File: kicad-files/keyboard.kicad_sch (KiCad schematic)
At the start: 148 parts, among them J1 TYPE-C-31-M12_13, U1 STM32F103x8_B-LQFP48

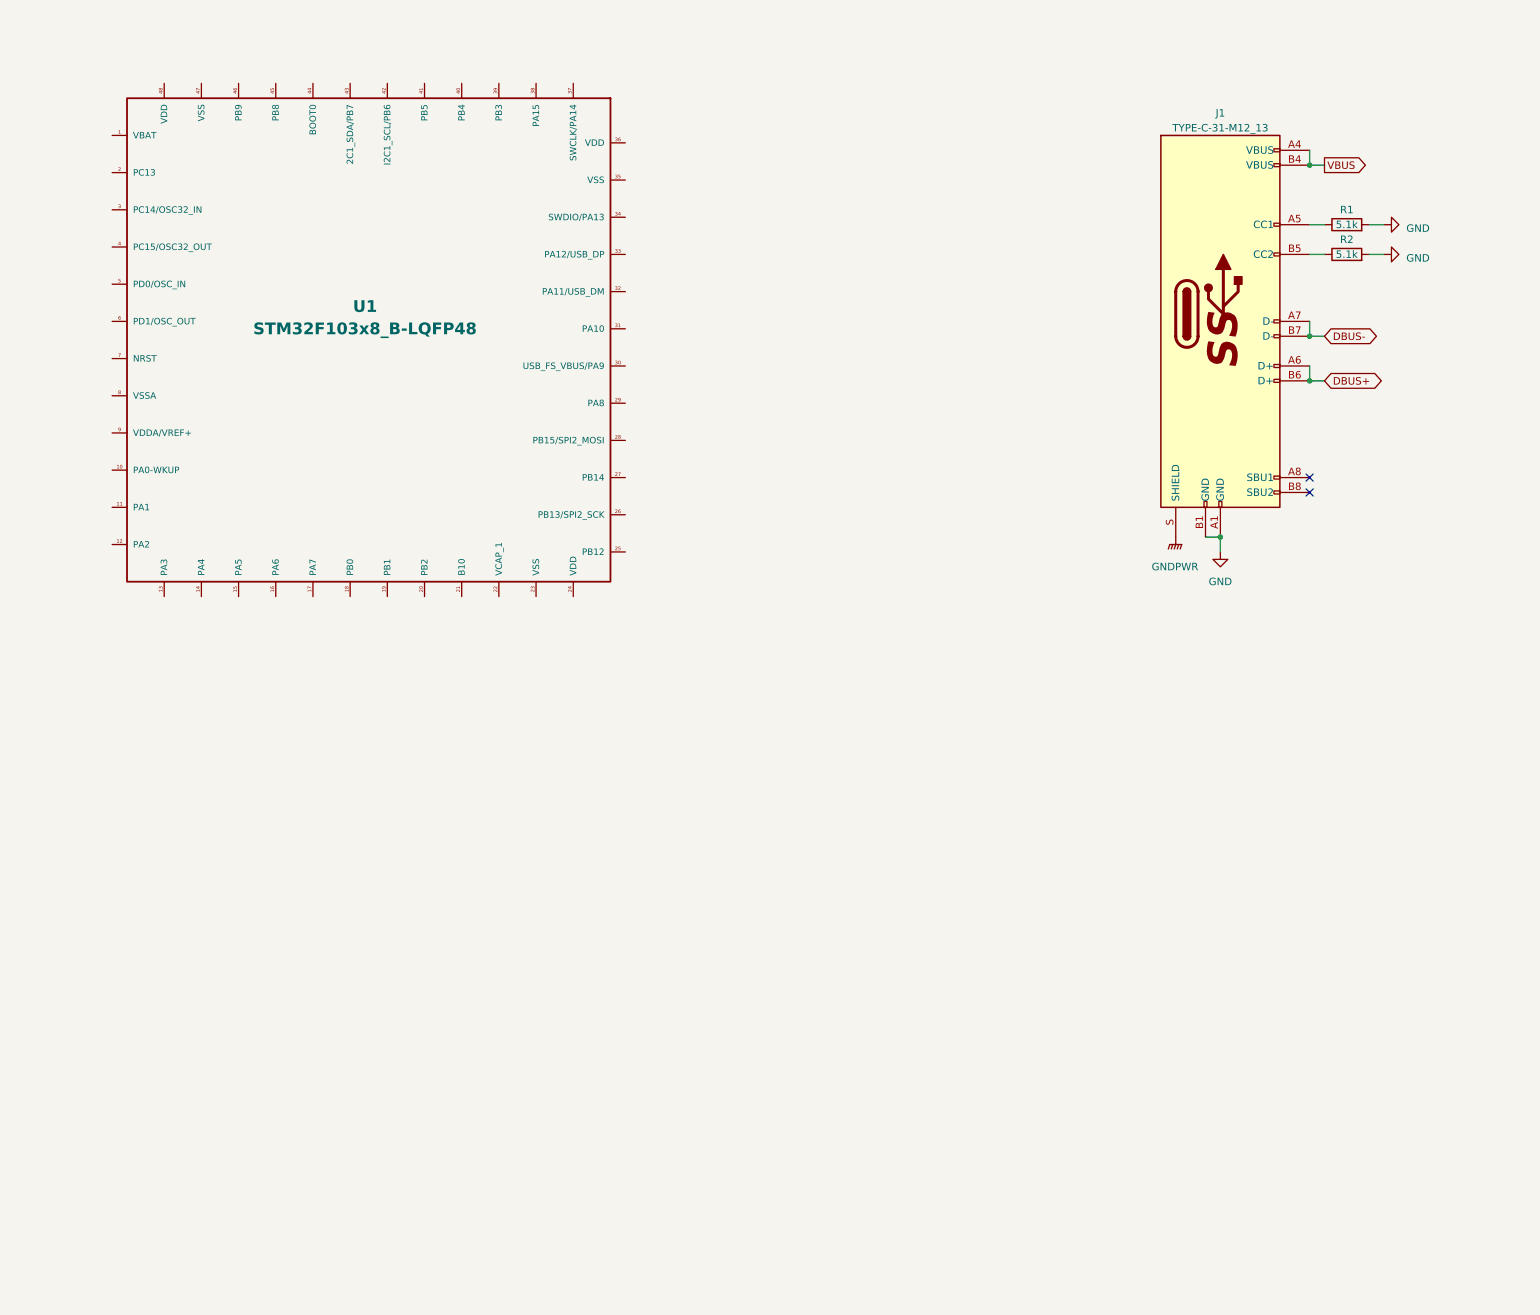
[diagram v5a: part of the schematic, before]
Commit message: Connected usb GNDPWR to inductor
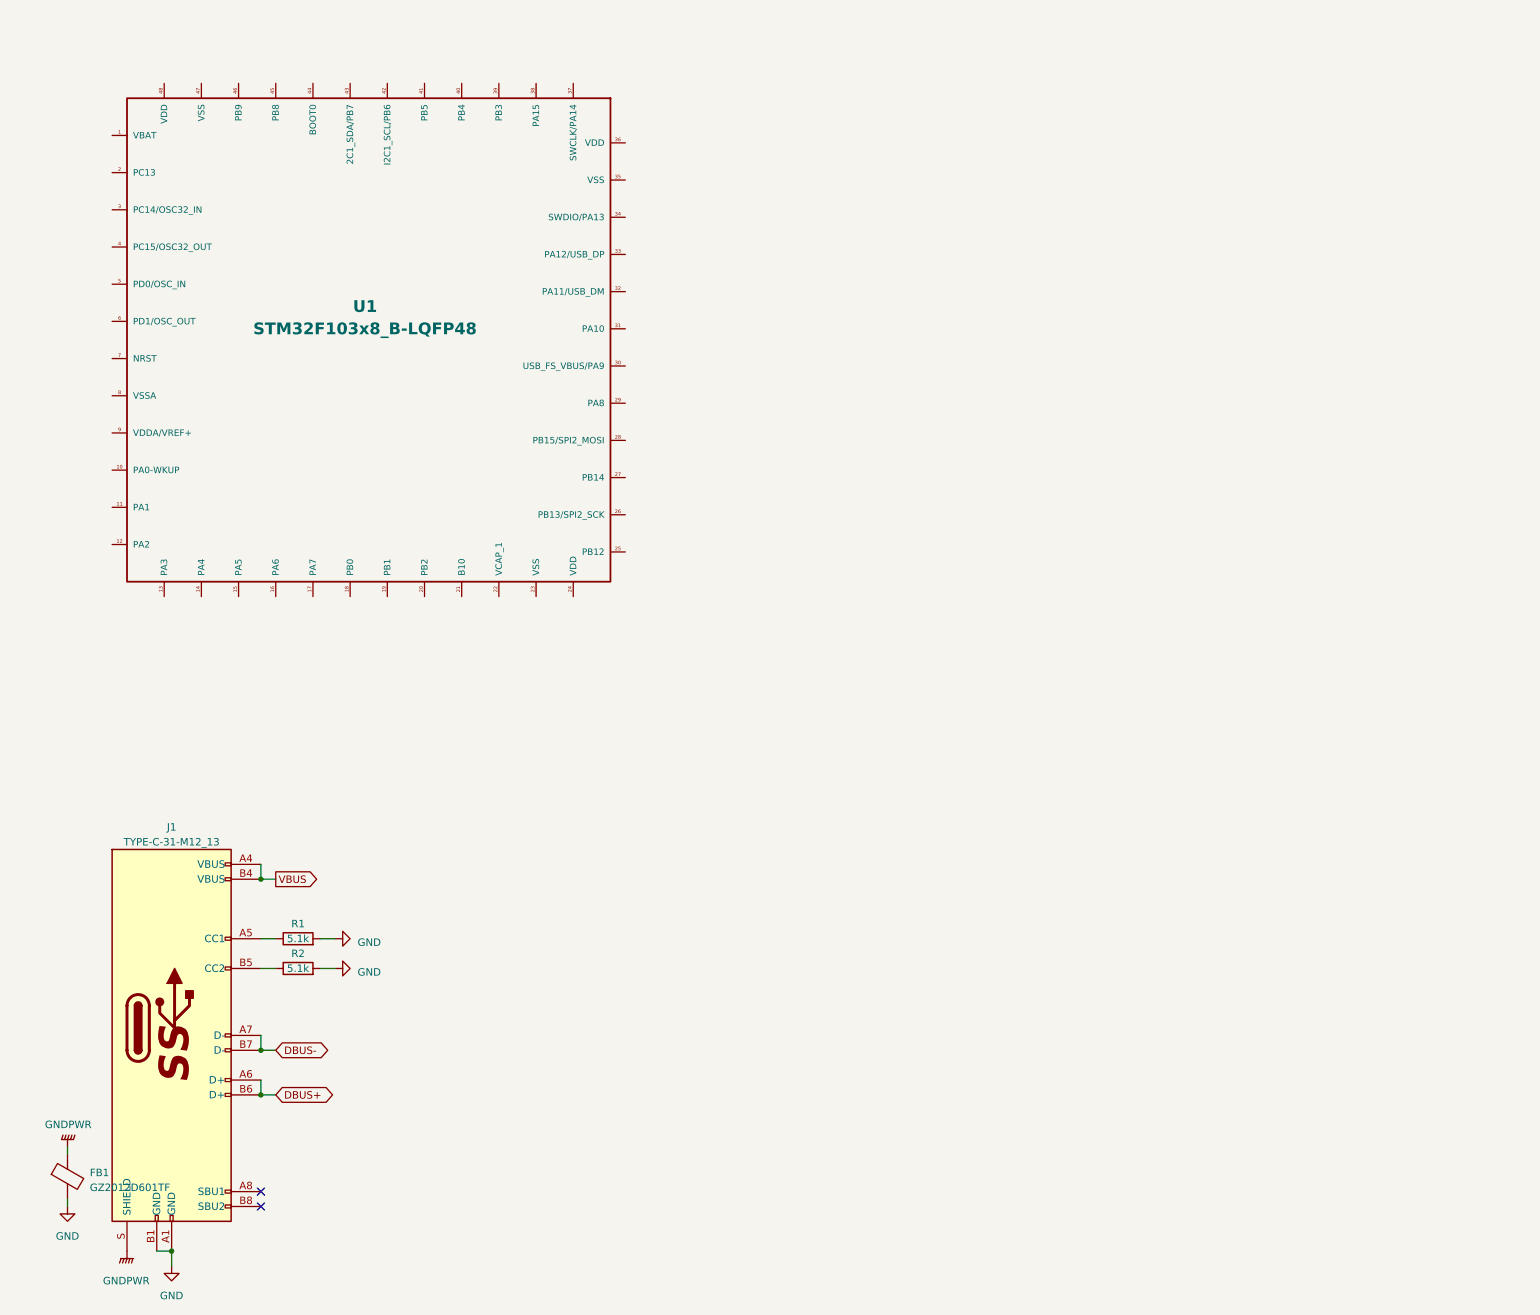
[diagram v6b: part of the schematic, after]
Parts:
- added FB1: GZ2012D601TF, Inductor_SMD:L_0805_2012Metric_Pad1.05x1.20mm_HandSolder, symbol Device:FerriteBead
- R1, R2: footprint Resistor_SMD:R_0805_2012Metric -> Resistor_SMD:R_0603_1608Metric
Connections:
- net GND: now also FB1.2
- net GNDPWR: now also FB1.1
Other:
- moved on the sheet: J1, R1, R2

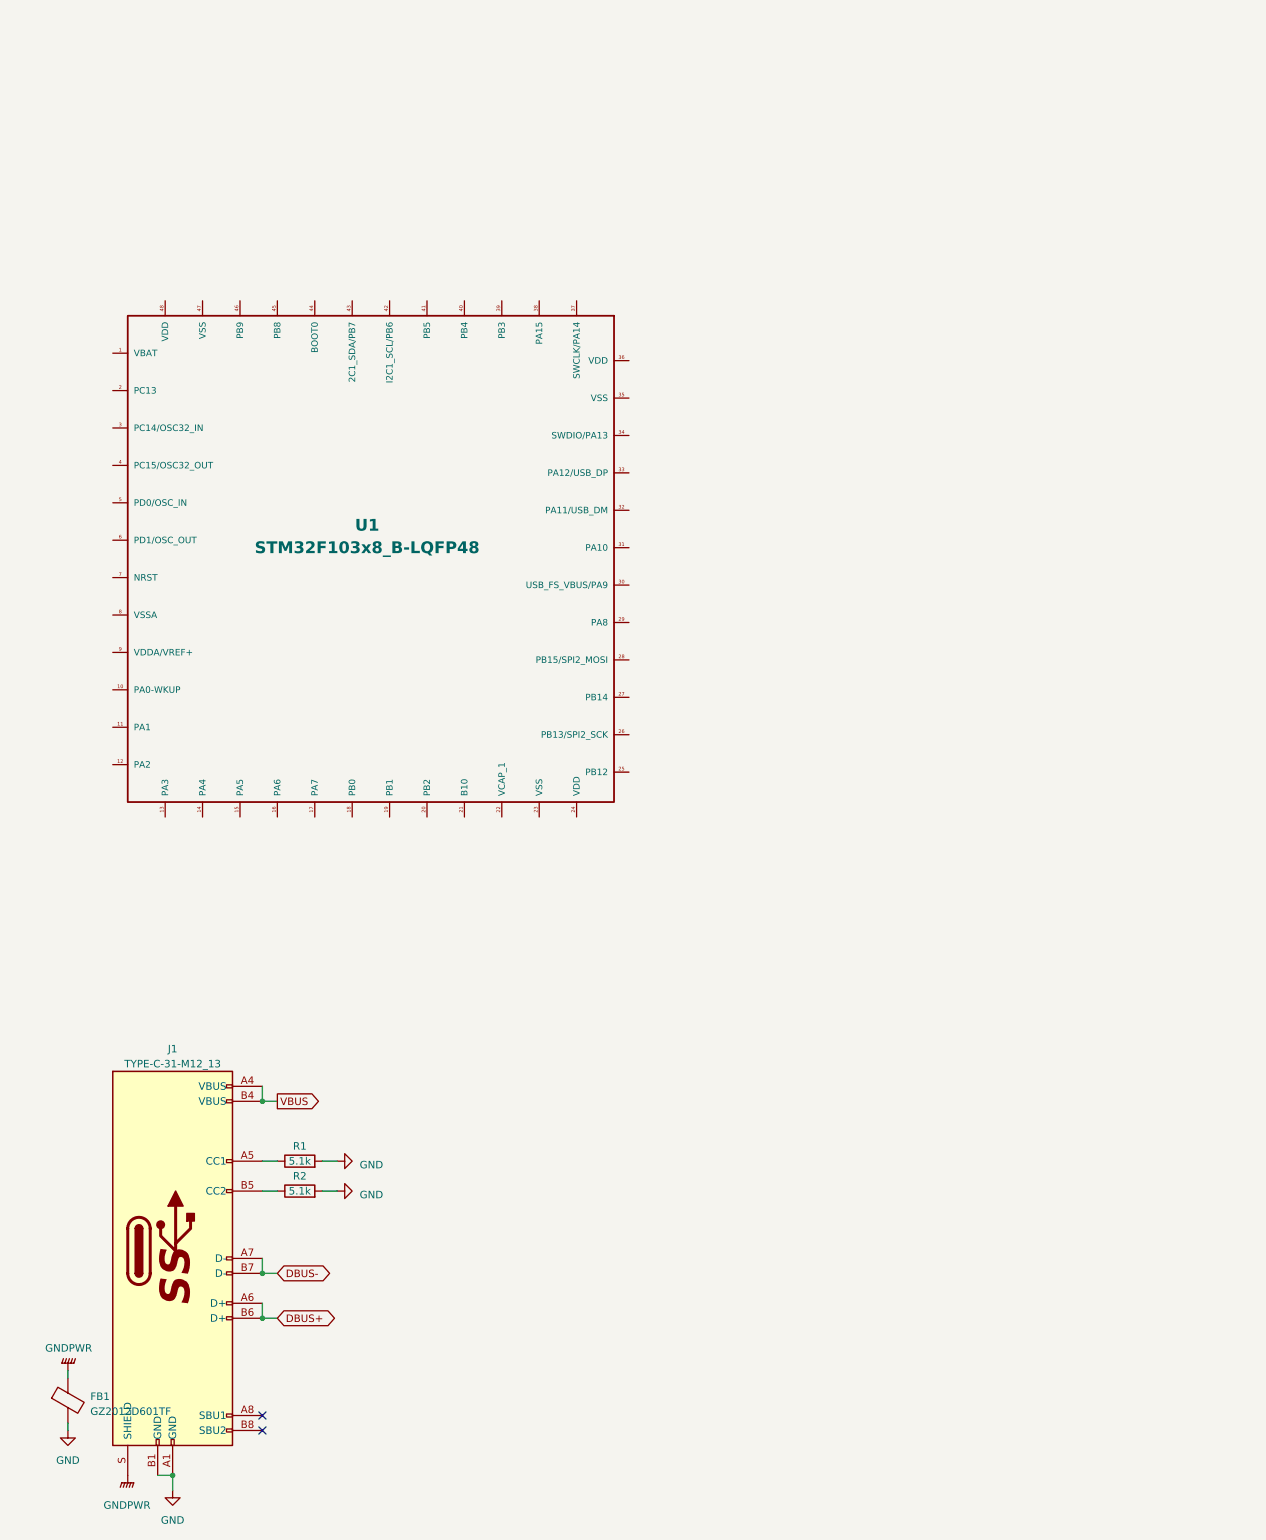
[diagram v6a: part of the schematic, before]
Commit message: Connected the 3V3 regulator & ESD Protection
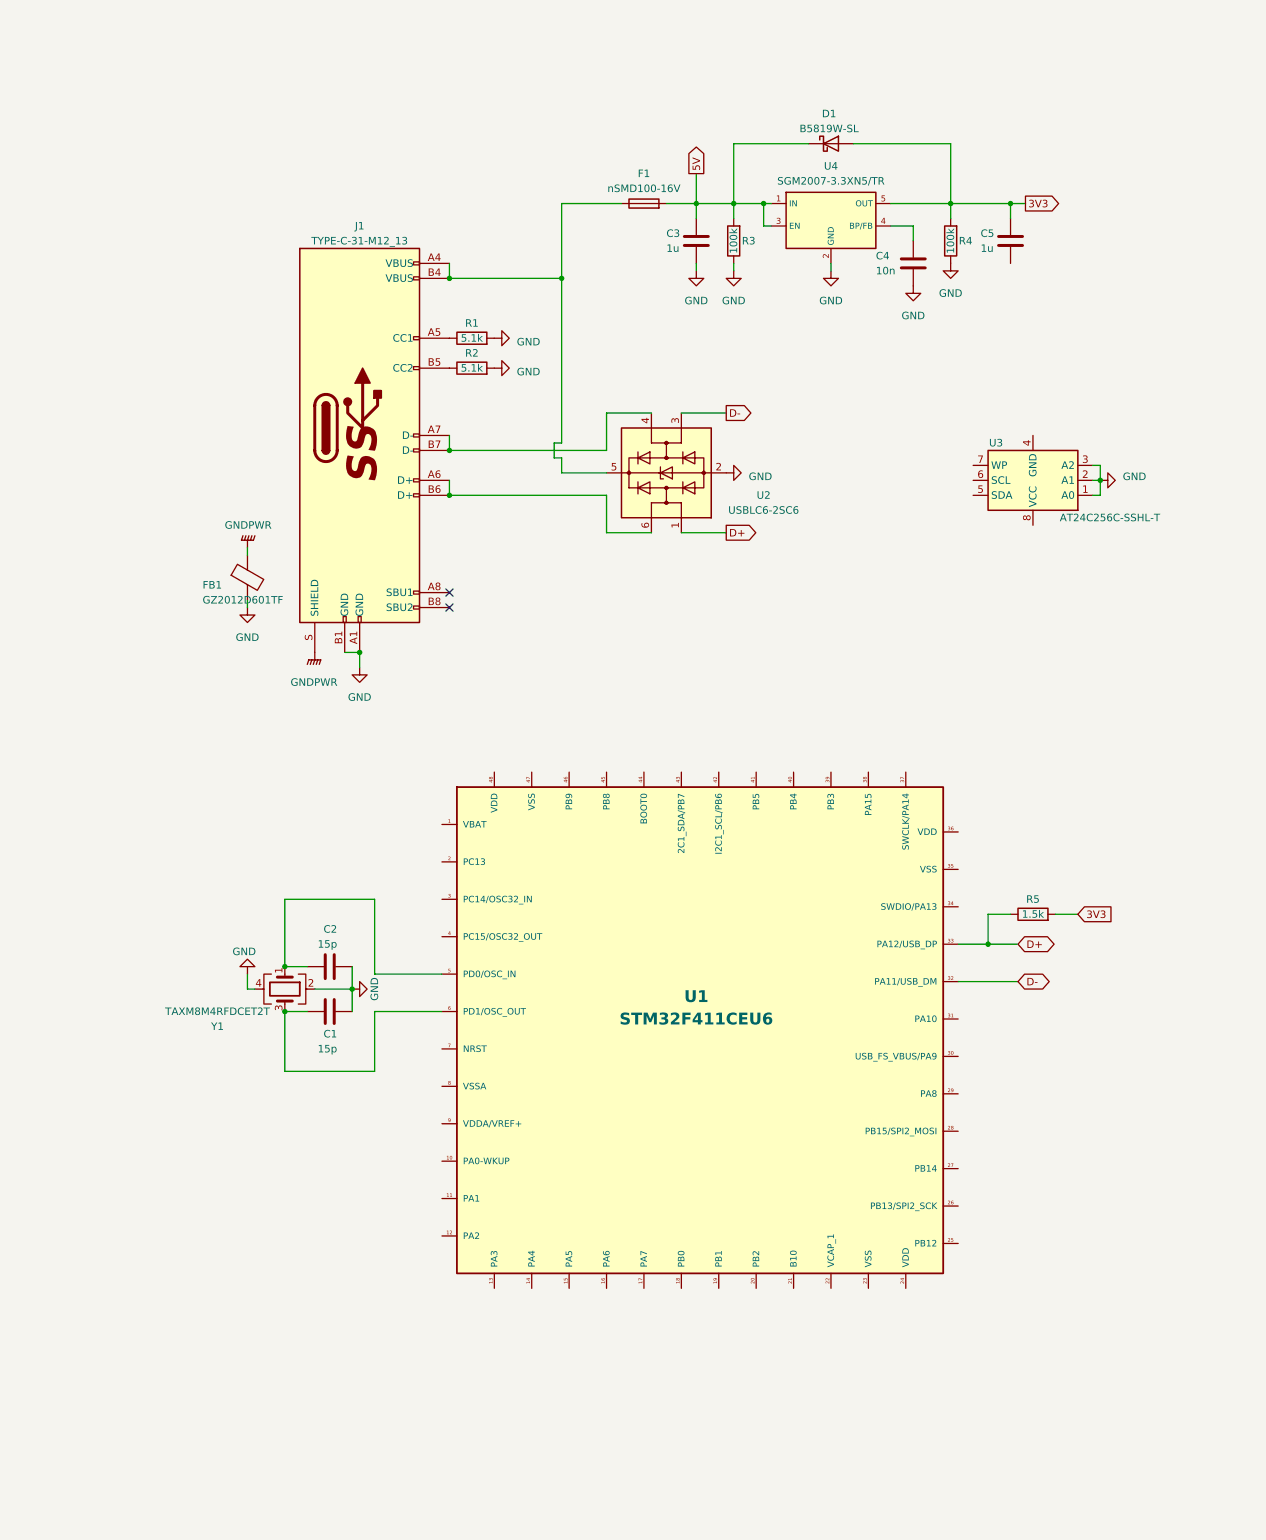
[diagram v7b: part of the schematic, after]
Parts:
- added C1, C2: 15p, Capacitor_SMD:C_0603_1608Metric_Pad1.08x0.95mm_HandSolder, symbol Device:C
- added C3, C5: 1u, Capacitor_SMD:C_0603_1608Metric_Pad1.08x0.95mm_HandSolder, symbol Device:C
- added C4: 10n, Capacitor_SMD:C_0603_1608Metric_Pad1.08x0.95mm_HandSolder, symbol Device:C
- added D1: B5819W-SL, Diode_SMD:D_SOD-123, symbol Device:D_Schottky
- added F1: nSMD100-16V, Fuse:Fuse_1206_3216Metric, symbol Device:Fuse
- added R3, R4: 100k, Resistor_SMD:R_0603_1608Metric, symbol Device:R
- added R5: 1.5k, Resistor_SMD:R_0603_1608Metric, symbol Device:R
- added U2: USBLC6-2SC6, acheron_Components:SOT-23-6, symbol Power_Protection:USBLC6-2SC6
- added U3: AT24C256C-SSHL-T, acheron_Components:TSSOP-8_4.4x3mm_P0.65mm, symbol Memory_EEPROM:24LC256
- added U4: SGM2007-3.3XN5/TR, acheron_Components:SOT-23-5, symbol acheron_Symbols:SGM2036
- added Y1: TAXM8M4RFDCET2T, acheron_Components:Crystal_SMD_3225-4Pin_3.2x2.5mm, symbol Device:Crystal_GND24
- U1: value STM32F103x8_B-LQFP48 -> STM32F411CEU6; Part Number (none) -> STM32F411
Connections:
- net GND: now also C1.2, C2.2, C3.2, C4.2, R3.1, R4.1, U2.2 (GND), U3.1 (A0), U3.2 (A1), U3.3 (A2), U4.2 (GND), Y1.2, Y1.4
- net D-: now reaches U1.32 (PA11/USB_DM)
- net D-: now also U2.3 (I/O2)
- net D+: now reaches U1.33 (PA12/USB_DP)
- net D+: now also R5.1, U2.1 (I/O1)
- net at U1.5 (PD0/OSC_IN): now also C2.1, Y1.1
- net at U1.6 (PD1/OSC_OUT): now also C1.1, Y1.3
- net DBUS+: no longer names the net of J1.A6 (D+), J1.B6 (D+)
- net DBUS+: now also U2.6 (I/O1)
- net DBUS-: no longer names the net of J1.A7 (D-), J1.B7 (D-)
- net DBUS-: now also U2.4 (I/O2)
- net VBUS: no longer names the net of J1.A4 (VBUS), J1.B4 (VBUS)
- net VBUS: now also F1.1, U2.5 (VBUS)
- new net: C4.1, U4.4 (BP/FB)
- new net 3V3: C5.1, D1.2 (A), R4.2, R5.2, U4.5 (OUT)
- new net 5V: C3.1, D1.1 (K), F1.2, R3.2, U4.1 (IN), U4.3 (EN)
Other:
- company: (none) -> Jemmec
- title: (none) -> legshark65 Ortholinear Keyboard
- moved on the sheet: FB1, J1, R1, R2
